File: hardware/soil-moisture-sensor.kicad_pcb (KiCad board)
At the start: 2 copper layers, 185.3 x 23 mm, 23 parts, among them J1 AVR ISP, J2 FTDI, SW1 SW_Push, U1 ATmega328P-AU, U2 NRF24L01_Breakout, U3 ATSHA204A, Y1 Resonator

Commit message: refactor(KiCad)!: Switch to KiCad 6 file layout
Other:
- net class Default removed
- net class POWER removed
- net class Sensor removed

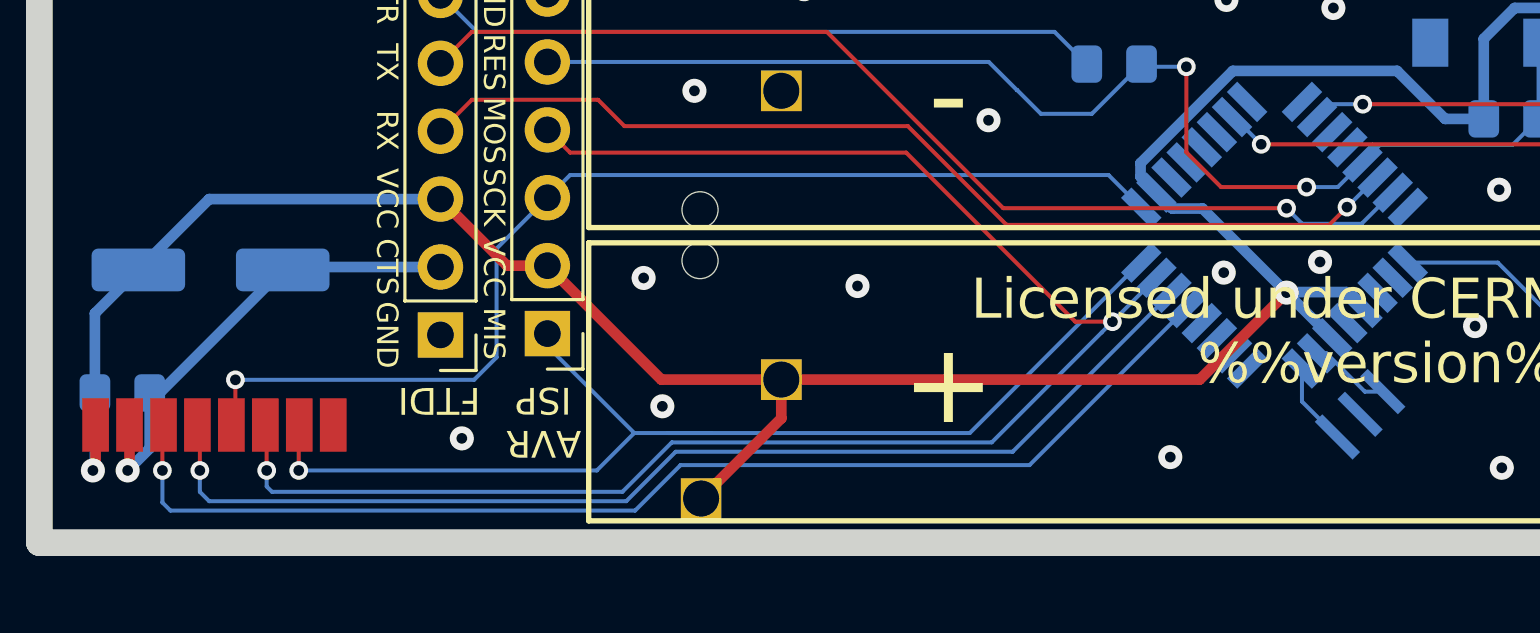
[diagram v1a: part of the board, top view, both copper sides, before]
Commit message: fix(PCB): Remove micro tracks
From the migration to KiCad 6 there were micro tracks producing errors in the
DRC.
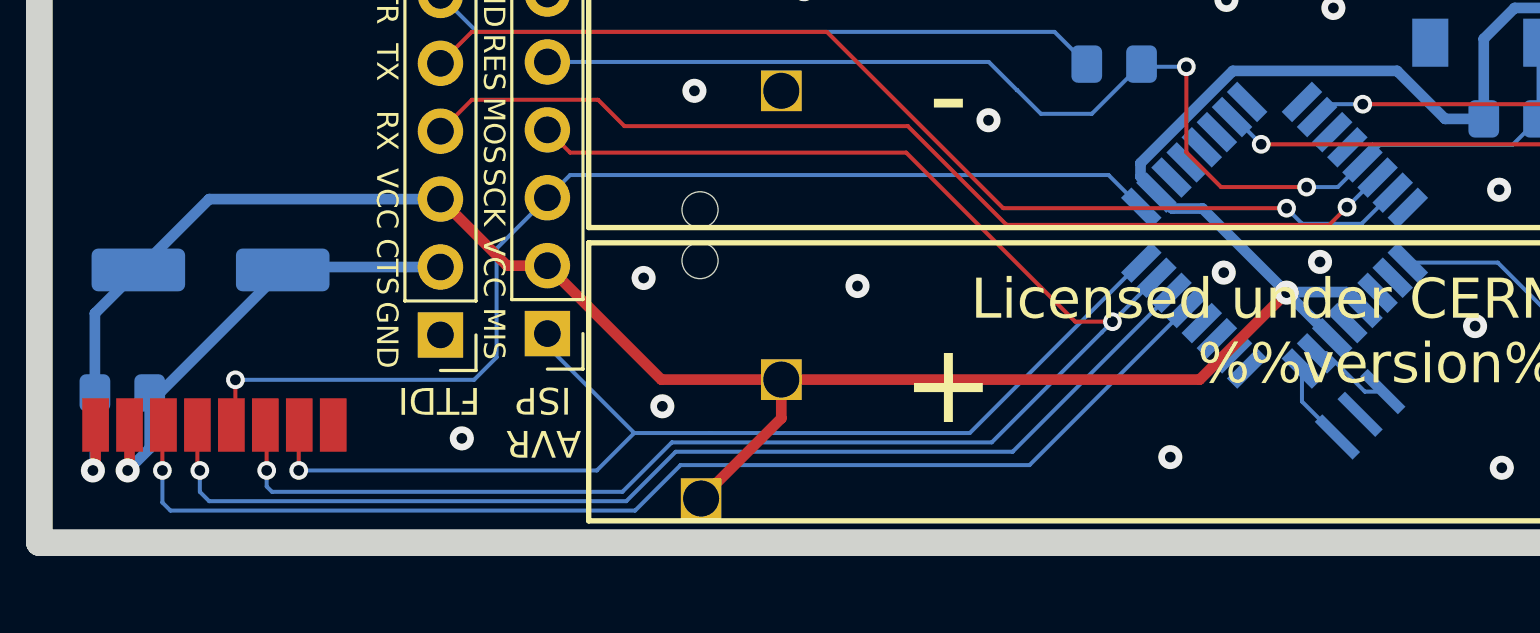
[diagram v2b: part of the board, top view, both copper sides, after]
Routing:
- net MISO: track 43.1 -> 41.5 mm
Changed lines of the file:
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@@
   (segment (start 75 121.32) (end 75.02 121.3) (width 0.15) (layer "F.Cu") (net 3))
   (segment (start 75 123) (end 75 121.32) (width 0.15) (layer "F.Cu") (net 3))
-  (segment (start 75.02 122.98) (end 75 123) (width 0.15) (layer "F.Cu") (net 3))
   (via (at 75 123) (size 0.7) (drill 0.4) (layers "F.Cu" "B.Cu") (net 3))
   (segment (start 84.3 118.35) (end 84.3 117.88) (width 0.15) (layer "B.Cu") (net 3))
   (segment (start 86.15 123) (end 75 123) (width 0.15) (layer "B.Cu") (net 3))
-  (segment (start 90.39998 121.59998) (end 88.810044 121.59998) (width 0.15) (layer "B.Cu") (net 3))
   (segment (start 87.54998 121.60002) (end 86.15 123) (width 0.15) (layer "B.Cu") (net 3))
   (segment (start 90.39998 121.59998) (end 87.54998 121.59998) (width 0.15) (layer "B.Cu") (net 3))
@@
   (segment (start 97.719999 111.109999) (end 85.149999 111.109999) (width 0.15) (layer "F.Cu") (net 5))
   (segment (start 104.045787 117.435787) (end 97.719999 111.109999) (width 0.15) (layer "F.Cu") (net 5))
-  (segment (start 73.75 122.95) (end 73.8 123) (width 0.15) (layer "F.Cu") (net 5))
   (segment (start 85.149999 111.109999) (end 84.3 110.26) (width 0.15) (layer "F.Cu") (net 5))
   (segment (start 73.8 123) (end 73.8 121.35) (width 0.15) (layer "F.Cu") (net 5))
@@
   (segment (start 102.76 109.66) (end 104.665 109.66) (width 0.15) (layer "B.Cu") (net 6))
   (segment (start 121.375 107.1) (end 121.475 107) (width 0.15) (layer "B.Cu") (net 6))
-  (segment (start 114.788047 111.477639) (end 114.722361 111.477639) (width 0.15) (layer "B.Cu") (net 6))
   (segment (start 121.375 109.85) (end 121.375 107.1) (width 0.15) (layer "B.Cu") (net 6))
   (segment (start 104.665 109.66) (end 106.525 107.8) (width 0.15) (layer "B.Cu") (net 6))
@@
   (segment (start 112.525305 120.422361) (end 113.851472 121.748528) (width 0.15) (layer "B.Cu") (net 9))
   (segment (start 112.525305 119.185103) (end 112.525305 120.422361) (width 0.15) (layer "B.Cu") (net 9))
-  (segment (start 69.94 122.96) (end 69.9 123) (width 0.15) (layer "F.Cu") (net 10))
   (segment (start 69.9 123) (end 69.9 121.34) (width 0.15) (layer "F.Cu") (net 10))
   (segment (start 69.9 121.34) (end 69.94 121.3) (width 0.15) (layer "F.Cu") (net 10))
@@
   (segment (start 70.2 124.5) (end 69.9 124.2) (width 0.15) (layer "B.Cu") (net 10))
   (segment (start 108.211953 116.922361) (end 102.334314 122.8) (width 0.15) (layer "B.Cu") (net 10))
-  (segment (start 71.21 122.91) (end 71.3 123) (width 0.15) (layer "F.Cu") (net 11))
-  (segment (start 71.3 123) (end 71.3 121.39) (width 0.15) (layer "F.Cu") (net 11))
-  (segment (start 71.3 121.39) (end 71.21 121.3) (width 0.15) (layer "F.Cu") (net 11))
+  (segment (start 71.21 122.91) (end 71.21 121.3) (width 0.15) (layer "F.Cu") (net 11))
+  (segment (start 71.3 123) (end 71.21 122.91) (width 0.15) (layer "F.Cu") (net 11))
   (via (at 71.3 123) (size 0.7) (drill 0.4) (layers "F.Cu" "B.Cu") (net 11))
+  (segment (start 71.3 123.8) (end 71.3 123) (width 0.15) (layer "B.Cu") (net 11))
   (segment (start 71.64999 124.14999) (end 71.3 123.8) (width 0.15) (layer "B.Cu") (net 11))
   (segment (start 101.702944 122.3) (end 89.1 122.3) (width 0.15) (layer "B.Cu") (net 11))
-  (segment (start 107.646268 116.356676) (end 101.702944 122.3) (width 0.15) (layer "B.Cu") (net 11))
+  (segment (start 101.702944 122.3) (end 107.646268 116.356676) (width 0.15) (layer "B.Cu") (net 11))
   (segment (start 87.25001 124.14999) (end 71.64999 124.14999) (width 0.15) (layer "B.Cu") (net 11))
-  (segment (start 71.3 123.8) (end 71.3 123) (width 0.15) (layer "B.Cu") (net 11))
   (segment (start 89.1 122.3) (end 87.25001 124.14999) (width 0.15) (layer "B.Cu") (net 11))
   (segment (start 81.475001 109.134999) (end 80.3 110.31) (width 0.15) (layer "F.Cu") (net 12))
@@
   (via (at 114.21 113.15) (size 0.7) (drill 0.4) (layers "F.Cu" "B.Cu") (net 12))
   (segment (start 115.316676 112.043324) (end 114.21 113.15) (width 0.15) (layer "B.Cu") (net 12))
-  (segment (start 115.353732 112.043324) (end 115.316676 112.043324) (width 0.15) (layer "B.Cu") (net 12))
-  (segment (start 115.353732 112.043324) (end 115.353732 112.046268) (width 0.15) (layer "B.Cu") (net 12))
   (segment (start 111.95 113.19) (end 101.35 113.19) (width 0.15) (layer "F.Cu") (net 13))
   (segment (start 94.754999 106.594999) (end 81.475001 106.594999) (width 0.15) (layer "F.Cu") (net 13))
@@
     (connect_pads (clearance 0.35))
     (min_thickness 0.254) (filled_areas_thickness no)
-    (fill (thermal_gap 0.508) (thermal_bridge_width 0.508))
+    (fill yes (thermal_gap 0.508) (thermal_bridge_width 0.508))
     (polygon
       (pts
@@
     (connect_pads (clearance 0.35))
     (min_thickness 0.254) (filled_areas_thickness no)
-    (fill (thermal_gap 0.508) (thermal_bridge_width 0.508))
+    (fill yes (thermal_gap 0.508) (thermal_bridge_width 0.508))
     (polygon
       (pts

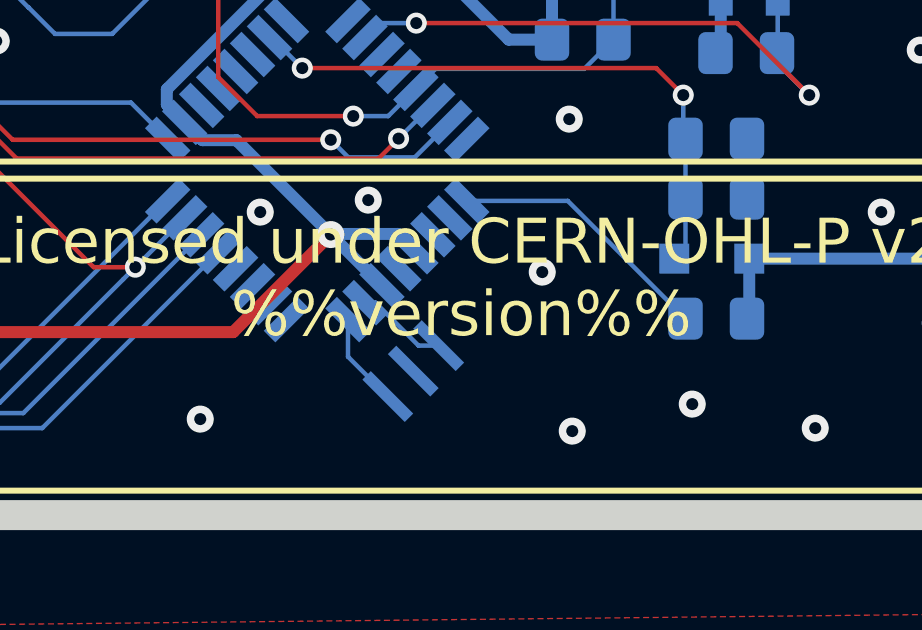
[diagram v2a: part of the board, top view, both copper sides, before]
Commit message: build: Switch to KiCad 6 text variables
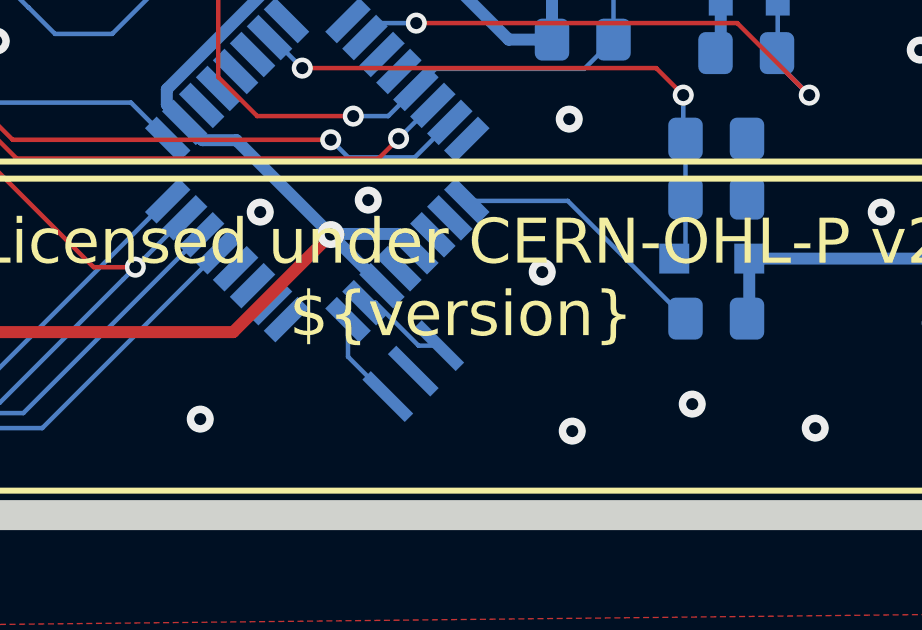
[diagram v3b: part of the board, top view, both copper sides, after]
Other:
- board text added: "Licensed under CERN-OHL-P v2 ${version}"
- board text removed: "Licensed under CERN-OHL-P v2 %%version%%"
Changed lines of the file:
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@@
   (paper "A4")
   (title_block
-    (date "2023-01-22")
-    (rev "%%version%%")
+    (date "${date}")
+    (rev "${version}")
   )
   (layers
@@
     (effects (font (size 1 1) (thickness 0.2)))
   )
-  (gr_text "Licensed under CERN-OHL-P v2\n%%version%%" (at 116.3 117.8) (layer "F.SilkS")
+  (gr_text "Licensed under CERN-OHL-P v2\n${version}" (at 116.3 117.8) (layer "F.SilkS")
     (effects (font (size 1.5 1.5) (thickness 0.3)))
   )
